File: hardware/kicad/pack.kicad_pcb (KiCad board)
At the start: 2 copper layers, 96 x 90 mm, 127 parts, among them U1 MT3608

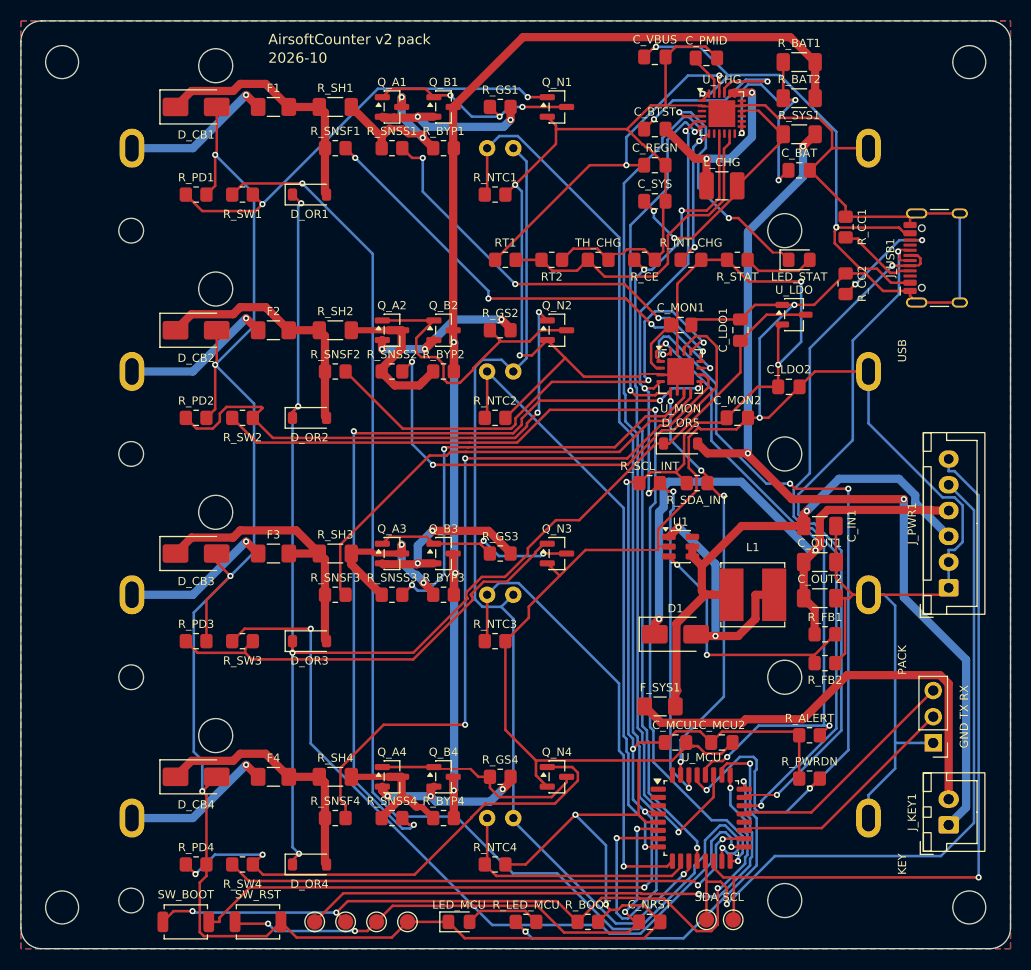
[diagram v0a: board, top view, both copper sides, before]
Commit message: hardware: 3D gate green with real models (carrier shifted 7 mm, plug keep-outs)
- assembly gate: _placed baked the board placement into the wrapper only, so some
  component solids stayed at the origin; now transform-copies keep their labels
- carrier shifted 7 mm toward x0 (CARRIER_SHIFT): the pack's right strip (J_UART1,
  J_PWR1, J_KEY1) clashed with the carrier underside and the Heltec socket pins
- Heltec envelope sized to the module (HELTEC_PCB around carrier.HELTEC_PADS)
- plug keep-outs (PLUG_REACH) above every top-entry XH header
- pack: J_KEY1 y77, J_UART1 y67.5, rerouted, DRC clean

Co-Authored-By: Claude Opus 5.5 <noreply@anthropic.com>
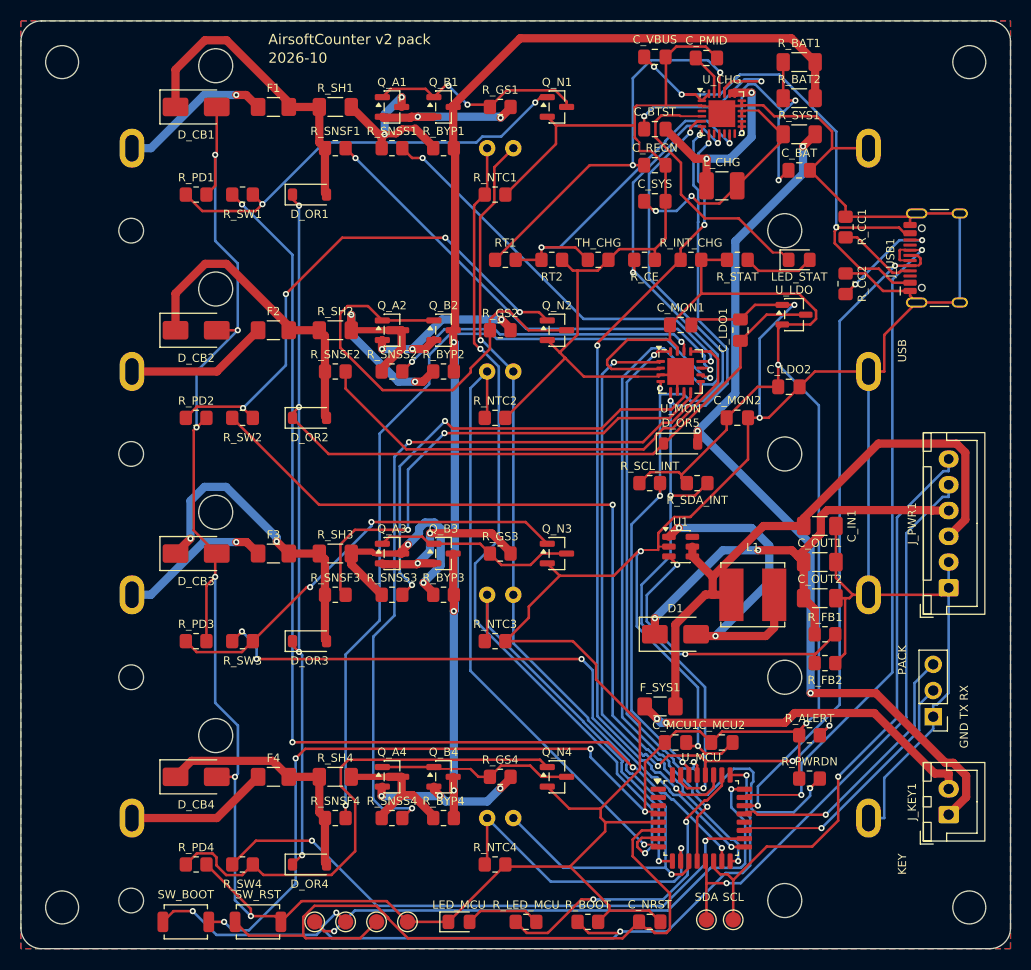
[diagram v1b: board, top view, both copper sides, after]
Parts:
- moved J_UART1 2.54 mm to (88.5, 67.5)
- moved J_KEY1 1.00 mm to (90.0, 77.0)
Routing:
- net GND: track 571.1 -> 546.5 mm
- net +3V3: track 171.6 -> 193.1 mm
- net NTC1: track 103.3 -> 82.0 mm, vias 1 -> 2
- net SNS_S2: track 51.2 -> 30.3 mm
- net CHG_INT: track 98.1 -> 77.6 mm, vias 3 -> 4
- net CHG_CE: track 79.6 -> 99.3 mm
- net SW1_DRV: track 120.3 -> 102.7 mm, vias 2 -> 4
- net SDA_EXT: track 70.6 -> 56.4 mm
- net NRST: track 54.5 -> 68.5 mm, vias 4 -> 0
- net SCL_EXT: track 73.0 -> 59.3 mm
- net CELL2_G: track 29.1 -> 42.7 mm
- net +5V: track 57.6 -> 44.1 mm
- net SW3_DRV: track 75.3 -> 62.3 mm, vias 2 -> 4
- net SW2_DRV: track 92.9 -> 81.2 mm
- net MON_PWRDN: track 81.2 -> 69.8 mm, vias 5 -> 3
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
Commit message: hardware: rebuild every board on KiCad 10.0.7 (fab outputs match the boards)
pack and pack_tme were re-routed by today's generators (the committed copper
was stale); the other boards only pick up a new GND_F zone uuid. Gerbers,
drill, BOM/CPL, schematic PDFs, renders and 1:1 prints regenerated for all 8
boards; ERC/DRC/gerber checks green. pack CPL: J_KEY1 Y follows the fresh
courtyard (-75.75).

Co-Authored-By: Claude Opus 5.5 <noreply@anthropic.com>
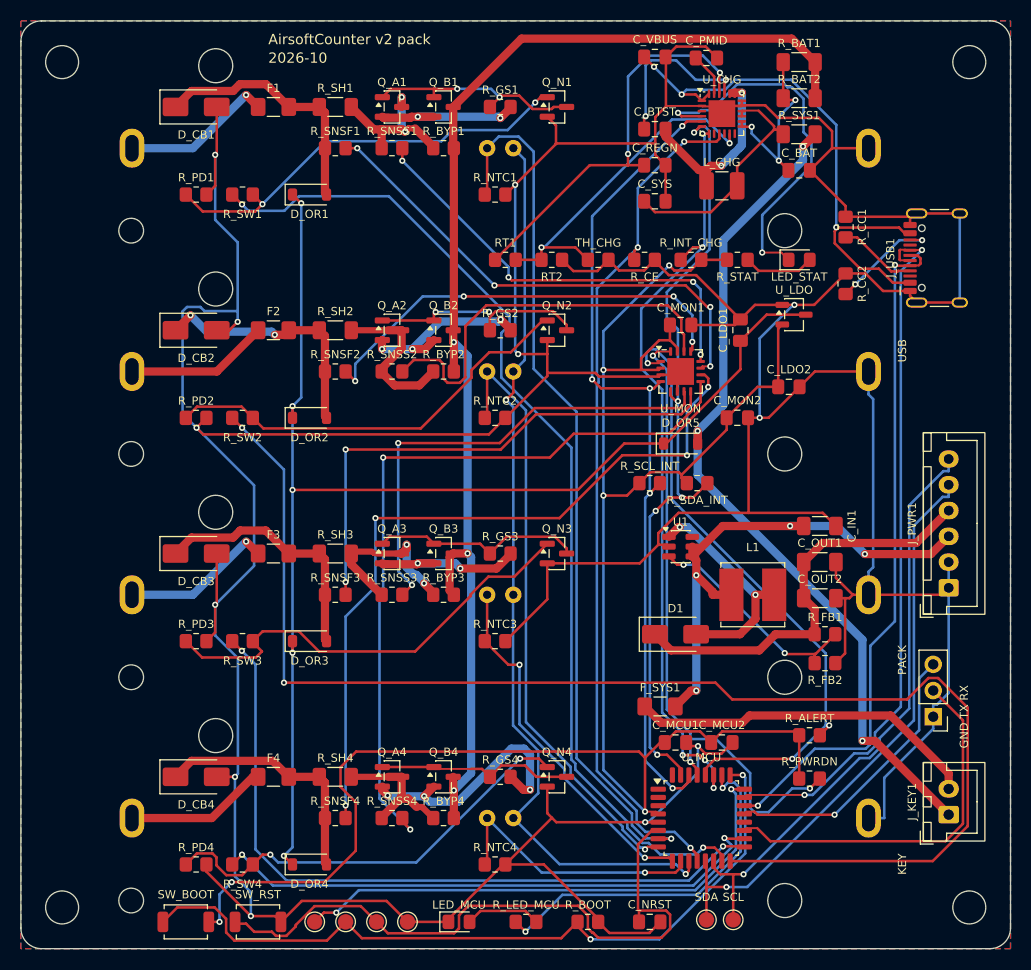
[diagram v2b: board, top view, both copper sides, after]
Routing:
- net SW2_DRV: track 81.2 -> 132.8 mm
- net GND: track 546.5 -> 569.1 mm, vias 10 -> 12
- net CELL2_G: track 42.7 -> 21.5 mm, vias 0 -> 2
- net CHG_CE: track 99.3 -> 84.5 mm
- net UART_TX: track 25.4 -> 36.6 mm, vias 1 -> 0
- net SW: track 32.9 -> 22.0 mm
- net STAT: track 26.0 -> 36.5 mm, vias 0 -> 2
- net NTC_PWR: track 99.2 -> 88.9 mm
- net SW2_G: track 51.1 -> 41.2 mm, vias 4 -> 0
- net VBAT_SW: track 59.5 -> 50.4 mm, vias 0 -> 4
- net SW3_DRV: track 62.3 -> 71.2 mm, vias 4 -> 2
- net CELL4_SRC: track 15.9 -> 24.7 mm
- net SNS_S2: track 30.3 -> 39.1 mm, vias 2 -> 0
- net CELL2_S: track 23.4 -> 15.9 mm, vias 2 -> 0
- net FB: track 29.1 -> 21.8 mm
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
